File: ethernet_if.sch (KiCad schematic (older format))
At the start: 23 parts, among them U6 ARJM11D7-114, U7 ENC424J600-PT, Y1 25MHz 50ppm

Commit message: Change for actual footprints, raff  board done.
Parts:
- D10, D11: value tbd -> B160-13-F; footprint Diode_SMD:D_0805_2012Metric_Pad1.15x1.40mm_HandSolder -> Diode_SMD:D_SMA_Handsoldering
- renumbered C18 to C19, C19 to C20, C20 to C21, C21 to C22, C22 to C23, C23 to C24, C24 to C25, C25 to C26, C26 to C27, R12 to R13, R13 to R14, R14 to R15, R15 to R16, R16 to R17, R17 to R18, R18 to R19, R19 to R20, R20 to R21
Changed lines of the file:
@@
 $EndComp
 $Comp
-L Device:C_Small C22
+L Device:C_Small C23
 U 1 1 60850C5F
 P 5850 4350
-F 0 "C22" V 5800 4250 50  0000 C CNN
+F 0 "C23" V 5800 4250 50  0000 C CNN
 F 1 "15p" V 5700 4250 50  0000 C CNN
 F 2 "Capacitor_SMD:C_0805_2012Metric_Pad1.18x1.45mm_HandSolder" H 5850 4350 50  0001 C CNN
@@
 $EndComp
 $Comp
-L Device:R_Small R17
+L Device:R_Small R18
 U 1 1 60850FC3
 P 5700 5450
-F 0 "R17" H 5759 5496 50  0000 L CNN
+F 0 "R18" H 5759 5496 50  0000 L CNN
 F 1 "12.4k,1%" H 5759 5405 50  0000 L CNN
 F 2 "Resistor_SMD:R_0805_2012Metric_Pad1.20x1.40mm_HandSolder" H 5700 5450 50  0001 C CNN
@@
 	7500 5450 7500 5550
 $Comp
-L Device:C_Small C26
+L Device:C_Small C27
 U 1 1 60851FEC
 P 7700 2550
-F 0 "C26" V 7471 2550 50  0000 C CNN
+F 0 "C27" V 7471 2550 50  0000 C CNN
 F 1 "0.1uF" V 7562 2550 50  0000 C CNN
 F 2 "Capacitor_SMD:C_0805_2012Metric_Pad1.18x1.45mm_HandSolder" H 7700 2550 50  0001 C CNN
@@
 $EndComp
 $Comp
-L Device:C_Small C25
+L Device:C_Small C26
 U 1 1 60852A51
 P 6200 5450
-F 0 "C25" H 6292 5496 50  0000 L CNN
+F 0 "C26" H 6292 5496 50  0000 L CNN
 F 1 "10uF" H 6292 5405 50  0000 L CNN
 F 2 "Capacitor_SMD:C_0805_2012Metric_Pad1.18x1.45mm_HandSolder" H 6200 5450 50  0001 C CNN
@@
 Connection ~ 6050 4350
 $Comp
-L Device:C_Small C23
+L Device:C_Small C24
 U 1 1 60863189
 P 5850 4550
-F 0 "C23" V 5800 4450 50  0000 C CNN
+F 0 "C24" V 5800 4450 50  0000 C CNN
 F 1 "15p" V 5700 4450 50  0000 C CNN
 F 2 "Capacitor_SMD:C_0805_2012Metric_Pad1.18x1.45mm_HandSolder" H 5850 4550 50  0001 C CNN
@@
 $EndComp
 $Comp
-L Device:R_Small R18
+L Device:R_Small R19
 U 1 1 60871C47
 P 6000 3650
-F 0 "R18" V 5950 3500 50  0000 C CNN
+F 0 "R19" V 5950 3500 50  0000 C CNN
 F 1 "180" V 5950 3800 50  0000 C CNN
 F 2 "Resistor_SMD:R_0805_2012Metric_Pad1.20x1.40mm_HandSolder" H 6000 3650 50  0001 C CNN
@@
 $EndComp
 $Comp
-L Device:R_Small R19
+L Device:R_Small R20
 U 1 1 608728F5
 P 6000 3750
-F 0 "R19" V 5950 3600 50  0000 C CNN
+F 0 "R20" V 5950 3600 50  0000 C CNN
 F 1 "180" V 5950 3900 50  0000 C CNN
 F 2 "Resistor_SMD:R_0805_2012Metric_Pad1.20x1.40mm_HandSolder" H 6000 3750 50  0001 C CNN
@@
 E_INT
 $Comp
-L Device:R_Small R20
+L Device:R_Small R21
 U 1 1 60875859
 P 8250 2500
-F 0 "R20" H 8309 2546 50  0000 L CNN
+F 0 "R21" H 8309 2546 50  0000 L CNN
 F 1 "100k" H 8309 2455 50  0000 L CNN
 F 2 "Resistor_SMD:R_0805_2012Metric_Pad1.20x1.40mm_HandSolder" H 8250 2500 50  0001 C CNN
@@
 $EndComp
 $Comp
-L Device:C_Small C18
+L Device:C_Small C19
 U 1 1 60932EF7
 P 3700 4900
-F 0 "C18" H 3750 5000 50  0000 L CNN
+F 0 "C19" H 3750 5000 50  0000 L CNN
 F 1 "1000pF,2kV" H 3250 4800 50  0000 L CNN
 F 2 "Capacitor_SMD:C_0805_2012Metric_Pad1.18x1.45mm_HandSolder" H 3700 4900 50  0001 C CNN
@@
 	3650 4350 5200 4350
 $Comp
-L Device:R_Small R12
+L Device:R_Small R13
 U 1 1 6093EEA9
 P 3900 2800
-F 0 "R12" V 3850 2950 50  0000 C CNN
+F 0 "R13" V 3850 2950 50  0000 C CNN
 F 1 "50R,1%" V 3850 2500 50  0000 C CNN
 F 2 "Resistor_SMD:R_0805_2012Metric_Pad1.20x1.40mm_HandSolder" H 3900 2800 50  0001 C CNN
@@
 $EndComp
 $Comp
-L Device:C_Small C21
+L Device:C_Small C22
 U 1 1 60947342
 P 5800 3250
-F 0 "C21" V 5750 3150 50  0000 C CNN
+F 0 "C22" V 5750 3150 50  0000 C CNN
 F 1 "6.8nF,10%" V 5750 3500 50  0000 C CNN
 F 2 "Capacitor_SMD:C_0805_2012Metric_Pad1.18x1.45mm_HandSolder" H 5800 3250 50  0001 C CNN
@@
 $EndComp
 $Comp
-L Device:C_Small C24
+L Device:C_Small C25
 U 1 1 6094806D
 P 5900 3350
-F 0 "C24" V 5950 3250 50  0000 C CNN
+F 0 "C25" V 5950 3250 50  0000 C CNN
 F 1 "6.8nF,10%" V 5950 3600 50  0000 C CNN
 F 2 "Capacitor_SMD:C_0805_2012Metric_Pad1.18x1.45mm_HandSolder" H 5900 3350 50  0001 C CNN
@@
 	3650 3250 3700 3250
 $Comp
-L Device:C_Small C20
+L Device:C_Small C21
 U 1 1 6099DE91
 P 4550 2950
-F 0 "C20" V 4500 2850 50  0000 C CNN
+F 0 "C21" V 4500 2850 50  0000 C CNN
 F 1 "0.1uF" V 4500 3100 50  0000 C CNN
 F 2 "Capacitor_SMD:C_0805_2012Metric_Pad1.18x1.45mm_HandSolder" H 4550 2950 50  0001 C CNN
@@
 $EndComp
 $Comp
-L Device:R_Small R16
+L Device:R_Small R17
 U 1 1 6099E4BB
 P 4350 2600
-F 0 "R16" H 4409 2646 50  0000 L CNN
+F 0 "R17" H 4409 2646 50  0000 L CNN
 F 1 "10R, 1/12W,1%" H 4409 2555 50  0000 L CNN
 F 2 "Resistor_SMD:R_0805_2012Metric_Pad1.20x1.40mm_HandSolder" H 4350 2600 50  0001 C CNN
@@
 	3650 2750 3700 2750
 $Comp
-L Device:R_Small R13
+L Device:R_Small R14
 U 1 1 6093E55A
 P 3900 3100
-F 0 "R13" V 3950 3250 50  0000 C CNN
+F 0 "R14" V 3950 3250 50  0000 C CNN
 F 1 "50R,1%" V 3950 2800 50  0000 C CNN
 F 2 "Resistor_SMD:R_0805_2012Metric_Pad1.20x1.40mm_HandSolder" H 3900 3100 50  0001 C CNN
@@
 	4350 2950 4450 2950
 $Comp
-L Device:R_Small R15
+L Device:R_Small R16
 U 1 1 609BBBBE
 P 3900 3600
-F 0 "R15" V 3950 3750 50  0000 C CNN
+F 0 "R16" V 3950 3750 50  0000 C CNN
 F 1 "50R,1%" V 3950 3300 50  0000 C CNN
 F 2 "Resistor_SMD:R_0805_2012Metric_Pad1.20x1.40mm_HandSolder" H 3900 3600 50  0001 C CNN
@@
 $EndComp
 $Comp
-L Device:R_Small R14
+L Device:R_Small R15
 U 1 1 609BBED7
 P 3900 3300
-F 0 "R14" V 3850 3450 50  0000 C CNN
+F 0 "R15" V 3850 3450 50  0000 C CNN
 F 1 "50R,1%" V 3850 3000 50  0000 C CNN
 F 2 "Resistor_SMD:R_0805_2012Metric_Pad1.20x1.40mm_HandSolder" H 3900 3300 50  0001 C CNN
@@
 	3650 3450 4050 3450
 $Comp
-L Device:C_Small C19
+L Device:C_Small C20
 U 1 1 609BF4B0
 P 4500 3450
-F 0 "C19" V 4450 3350 50  0000 C CNN
+F 0 "C20" V 4450 3350 50  0000 C CNN
 F 1 "0.1uF" V 4450 3600 50  0000 C CNN
 F 2 "Capacitor_SMD:C_0805_2012Metric_Pad1.18x1.45mm_HandSolder" H 4500 3450 50  0001 C CNN
@@
 P 3850 3800
 F 0 "D10" H 3950 3750 50  0000 C CNN
-F 1 "tbd" H 3700 3750 50  0000 C CNN
-F 2 "Diode_SMD:D_0805_2012Metric_Pad1.15x1.40mm_HandSolder" V 3850 3800 50  0001 C CNN
+F 1 "B160-13-F" H 3550 3750 50  0000 C CNN
+F 2 "Diode_SMD:D_SMA_Handsoldering" V 3850 3800 50  0001 C CNN
 F 3 "~" V 3850 3800 50  0001 C CNN
 	1    3850 3800
@@
 P 3850 3900
 F 0 "D11" H 3950 3950 50  0000 C CNN
-F 1 "tbd" H 3700 3950 50  0000 C CNN
-F 2 "Diode_SMD:D_0805_2012Metric_Pad1.15x1.40mm_HandSolder" V 3850 3900 50  0001 C CNN
+F 1 "B160-13-F" H 3550 3950 50  0000 C CNN
+F 2 "Diode_SMD:D_SMA_Handsoldering" V 3850 3900 50  0001 C CNN
 F 3 "~" V 3850 3900 50  0001 C CNN
 	1    3850 3900

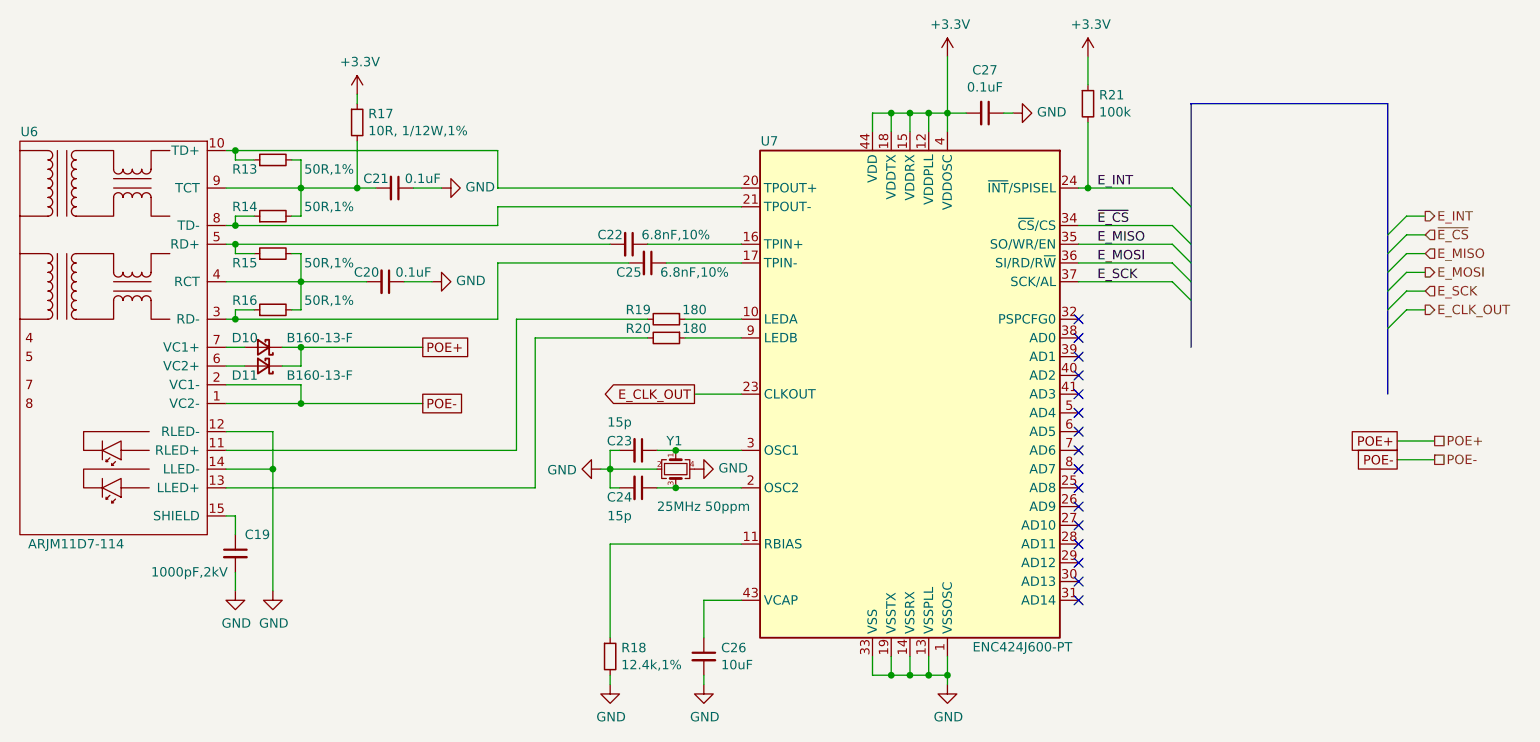
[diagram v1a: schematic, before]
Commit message: Connector placment done, dimentions decided ...
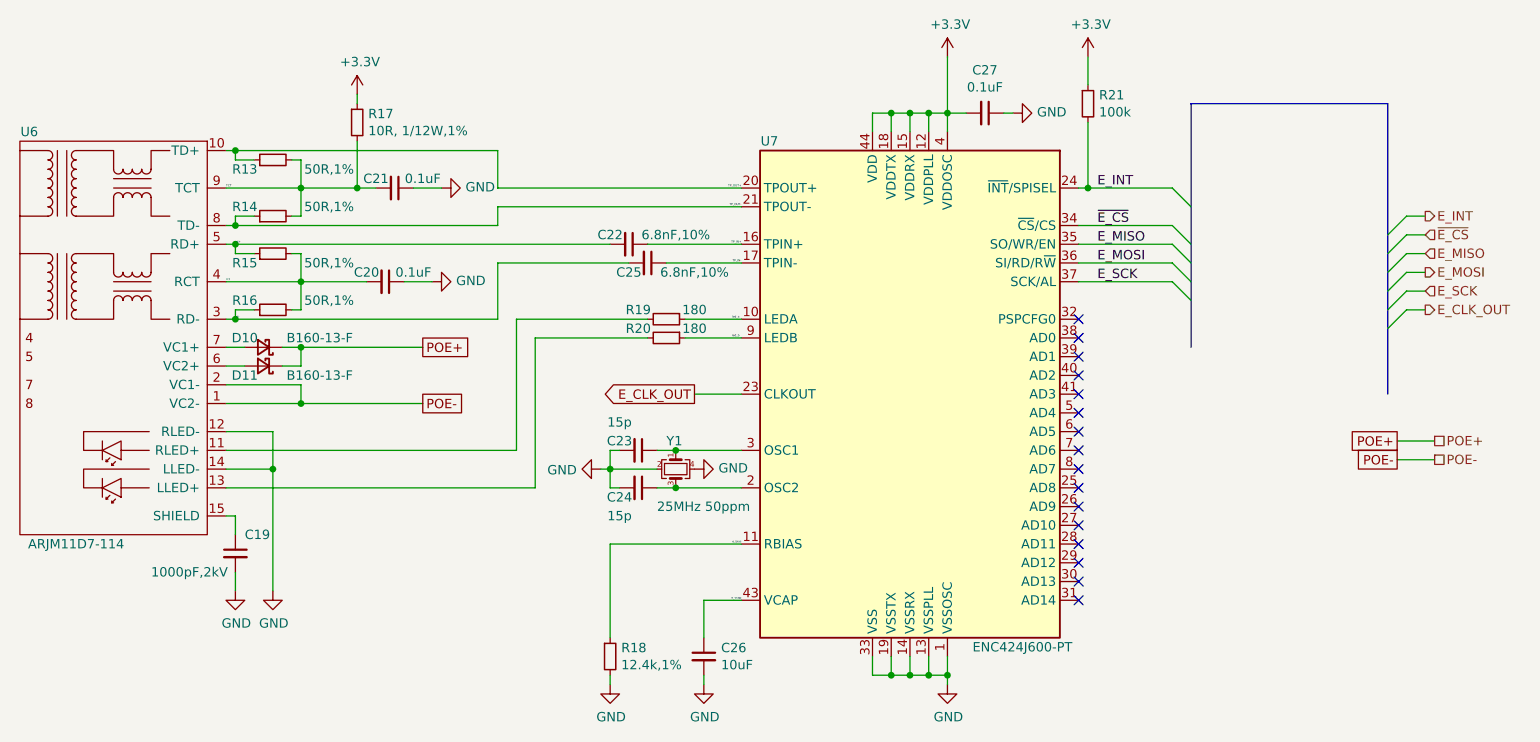
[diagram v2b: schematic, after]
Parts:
- Y1: footprint Crystal:Crystal_SMD_Abracon_ABM3B-4Pin_5.0x3.2mm -> Crystal:Crystal_SMD_3225-4Pin_3.2x2.5mm_HandSoldering
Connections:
- net led_a: now reaches R19.1, U7.10 (LEDA)
- net e_bias: now reaches R18.1, U7.11 (RBIAS)
- net TP_IN+: now reaches C22.1, U7.16 (TPIN+)
- net TP_IN-: now reaches C25.1, U7.17 (TPIN-)
- net TP_OUT+: now reaches R13.1, U6.10 (TD+), U7.20 (TPOUT+)
- net TP_OUT-: now reaches R14.1, U6.8 (TD-), U7.21 (TPOUT-)
- net e_vcap: now reaches C26.1, U7.43 (VCAP)
- net led_b: now reaches R20.1, U7.9 (LEDB)
- net rd-: now reaches C25.2, R16.1, U6.3 (RD-)
- net rct: now reaches C20.2, R15.2, R16.2, U6.4 (RCT)
- net rd+: now reaches C22.2, R15.1, U6.5 (RD+)
- net TCT: now reaches C21.2, R13.2, R14.2, R17.2, U6.9 (TCT)
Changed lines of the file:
@@
 F 0 "Y1" V 5900 4400 50  0000 L CNN
 F 1 "25MHz 50ppm" V 6250 4350 50  0000 L CNN
-F 2 "Crystal:Crystal_SMD_Abracon_ABM3B-4Pin_5.0x3.2mm" H 6050 4450 50  0001 C CNN
+F 2 "Crystal:Crystal_SMD_3225-4Pin_3.2x2.5mm_HandSoldering" H 6050 4450 50  0001 C CNN
 F 3 "~" H 6050 4450 50  0001 C CNN
 	1    6050 4450
@@
 Wire Bus Line
 	9850 2500 9850 4050
+Text Label 6350 3650 0    11   ~ 0
+led_a
+Text Label 6350 3750 0    11   ~ 0
+led_b
+Text Label 6400 2950 2    11   ~ 0
+TP_OUT+
+Text Label 6400 3050 2    11   ~ 0
+TP_OUT-
+Text Label 6400 3350 2    11   ~ 0
+TP_IN-
+Text Label 6400 3250 2    11   ~ 0
+TP_IN+
+Text Label 6400 4850 2    11   ~ 0
+e_bias
+Text Label 6400 5150 2    11   ~ 0
+e_vcap
+Text Label 3650 2950 0    11   ~ 0
+TCT
+Text Label 3700 3250 0    11   ~ 0
+rd+
+Text Label 3700 3650 0    11   ~ 0
+rd-
+Text Label 3650 3450 0    11   ~ 0
+rct
 $EndSCHEMATC
